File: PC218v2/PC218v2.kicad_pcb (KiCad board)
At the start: 2 copper layers, 104.2 x 29 mm, 49 parts, among them J1 PC218_BoardEdge_44pin, Q1 BC848W, Q10 BC848W, Q11 BC848W, Q12 BC848W, Q13 BC848W, Q14 BC848W, Q15 BC848W, Q2 BC848W, Q3 BC848W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

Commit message: PC218 Rev 2.1
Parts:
- added REF**: OSHW-Logo_11.4x12mm_SilkScreen, Symbol:OSHW-Logo_11.4x12mm_SilkScreen, B.Cu at (56.9, 56.4)
- J1: footprint keithley_615_part_library:PC218_Edge_Connector -> footprints:PC218_Edge_Connector
- moved J1 91.2 mm to (55.8, 78.0), turned to 0 degrees
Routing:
- net GND: track 8.05 -> 6.67 mm, vias 13 -> 17
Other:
- outline, holes or cut-outs redrawn
- board text added: "Keithley 615 PC218 Replacement V2.1 Peter Farley, 2023"
- board text removed: "Keithley 615 PC218 Replacement Peter Farley 2023"

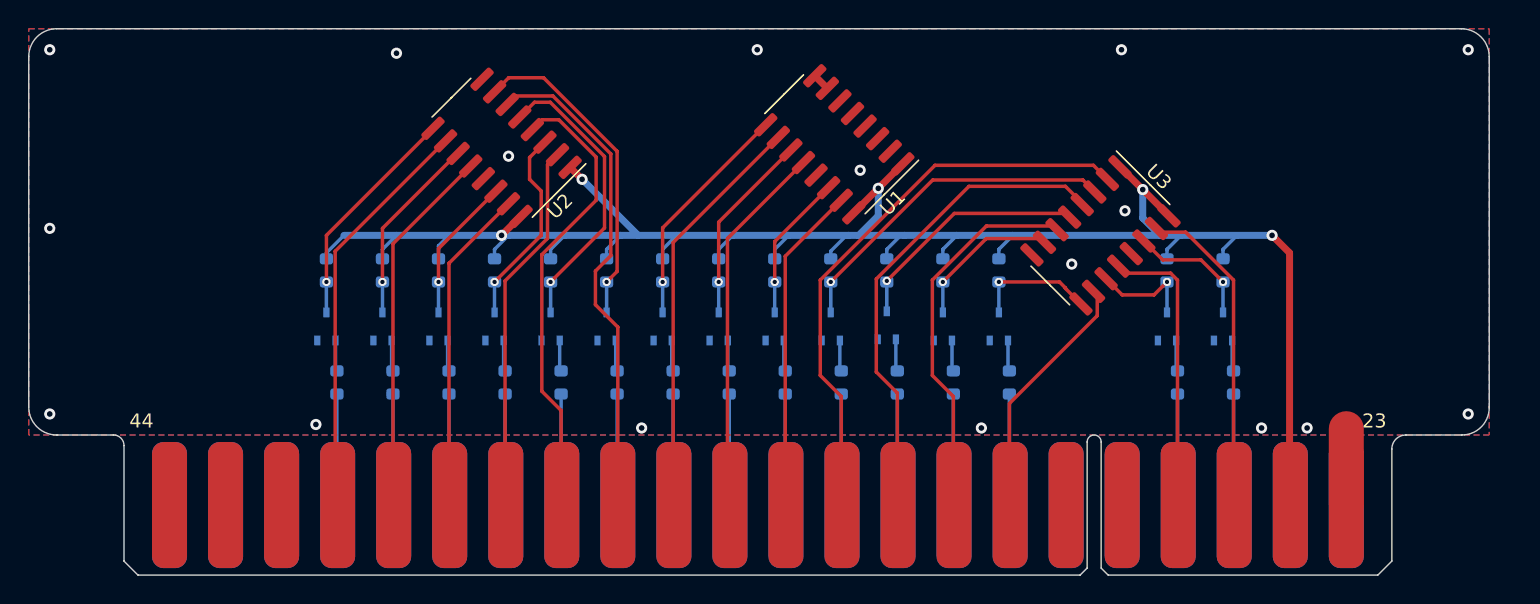
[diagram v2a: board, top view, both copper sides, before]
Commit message: PC218v2: Rev 2.2
Matched form factor of new PC209 board
Added power test points
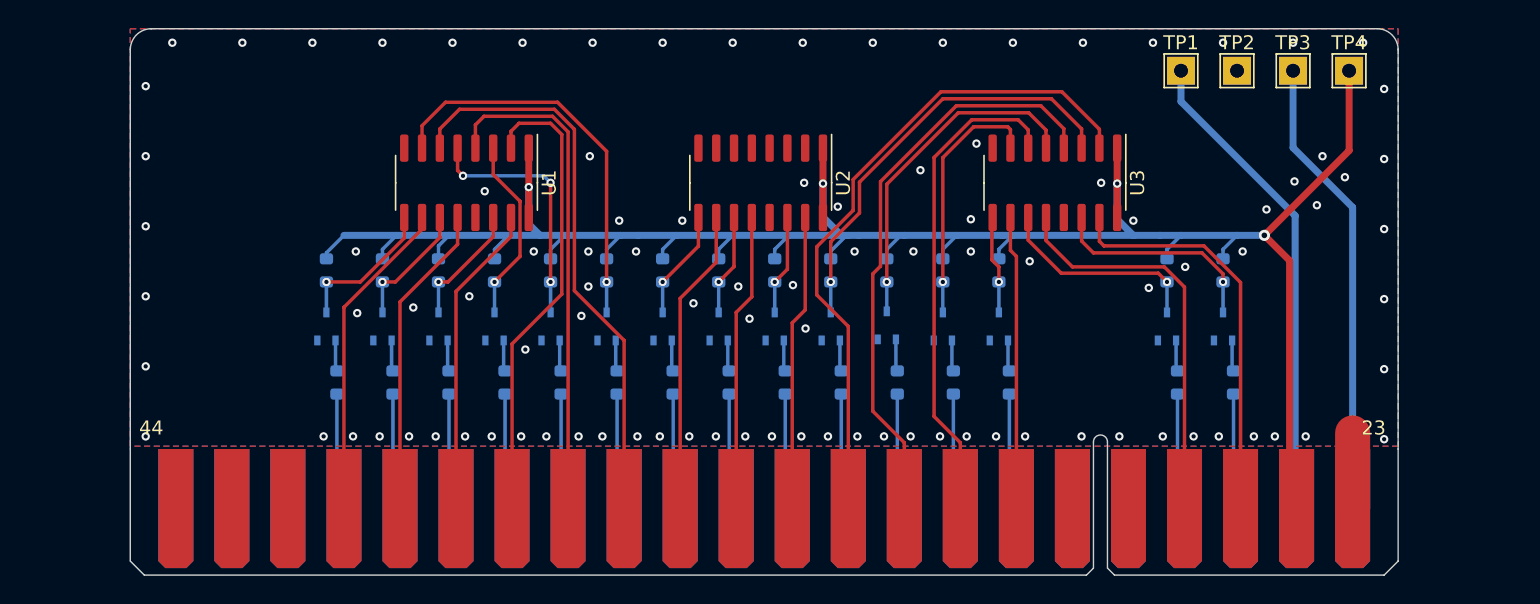
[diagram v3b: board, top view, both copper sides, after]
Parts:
- removed the REF** at (56.9, 56.4)
- added REF**: KiCad-Logo2_5mm_SilkScreen, Symbol:KiCad-Logo2_5mm_SilkScreen, B.Cu at (65.8, 53.8)
- added REF**: OSHW-Logo_5.7x6mm_SilkScreen, Symbol:OSHW-Logo_5.7x6mm_SilkScreen, B.Cu at (75.5, 53.8)
- added TP1: -15V, TestPoint:TestPoint_THTPad_2.0x2.0mm_Drill1.0mm, F.Cu at (132.0, 52.0)
- added TP2: GND, TestPoint:TestPoint_THTPad_2.0x2.0mm_Drill1.0mm, F.Cu at (136.0, 52.0)
- added TP3: 3.6V, TestPoint:TestPoint_THTPad_2.0x2.0mm_Drill1.0mm, F.Cu at (140.0, 52.0)
- added TP4: 15V, TestPoint:TestPoint_THTPad_2.0x2.0mm_Drill1.0mm, F.Cu at (144.0, 52.0)
- moved U2 5.93 mm to (102.0, 60.0), turned to -90 degrees
- moved U3 4.96 mm to (123.0, 60.0), turned to -90 degrees
- moved U1 3.54 mm to (81.0, 60.0), turned to -90 degrees
- moved J1 1.56 mm to (57.0, 79.0)
- renumbered U2 to U1, U1 to U2
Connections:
- J1 pad 1: unconnected-(J1-Pad1) -> +3.6V
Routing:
- net -15V: track 0.00 -> 34.7 mm
- net +3.6V: track 0.00 -> 33.0 mm
- net +15V: track 144.2 -> 158.8 mm, vias 5 -> 4
- net Net-(Q9-Pad3): track 16.4 -> 7.83 mm
- net Overload Print: track 20.7 -> 28.7 mm
- net 2x10^2 Print: track 27.3 -> 35.3 mm
- net Net-(Q2-Pad3): track 7.38 -> 14.9 mm
- net 1x10^0 Print: track 29.4 -> 21.8 mm
- net Net-(Q4-Pad3): track 10.8 -> 18.2 mm
- net 4x10^2 Print: track 41.0 -> 48.1 mm
- net 1x10^2 Print: track 34.8 -> 41.9 mm
- net Net-(Q5-Pad3): track 17.3 -> 24.4 mm
- net 8x10^1 Print: track 26.6 -> 33.6 mm
- net Net-(Q8-Pad3): track 13.7 -> 7.23 mm
- net Net-(Q1-Pad3): track 9.04 -> 15.5 mm
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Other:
- board size 104.2 x 29 mm -> 90.5 x 30 mm
- board text added: "+15V"
- board text added: "+3.6V"
- board text added: "-15V"
- board text added: "GND"
- board text added: "Keithley 615 PC218 Replacement V2.2 Peter Farley, 2023"
- board text removed: "Keithley 615 PC218 Replacement V2.1 Peter Farley, 2023"
